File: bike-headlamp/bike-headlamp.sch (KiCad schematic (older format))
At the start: 9 parts, among them P1 Harness Connection, P2 HEADSET, P3 LED1, P4 LED2, SW1 RED, SW2 WHITE, SW3 DIM, U1 BUCKPUCK-3021-D-E-700, U2 Trinket

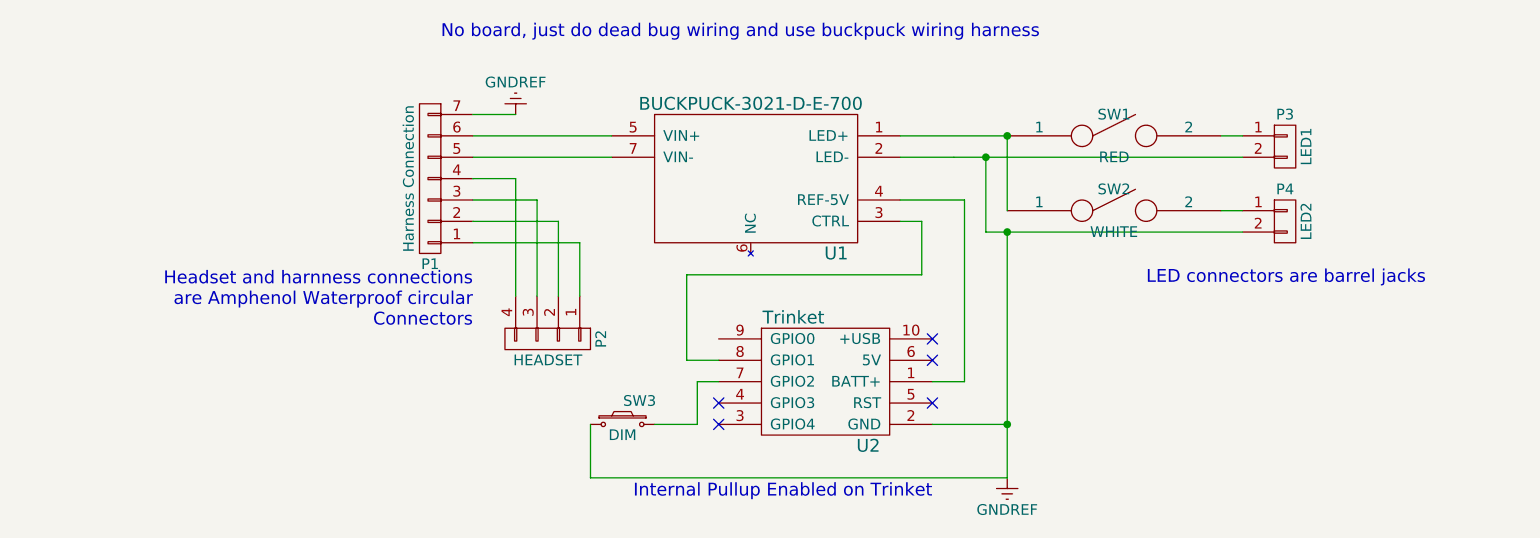
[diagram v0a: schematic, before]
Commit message: added strobe switch
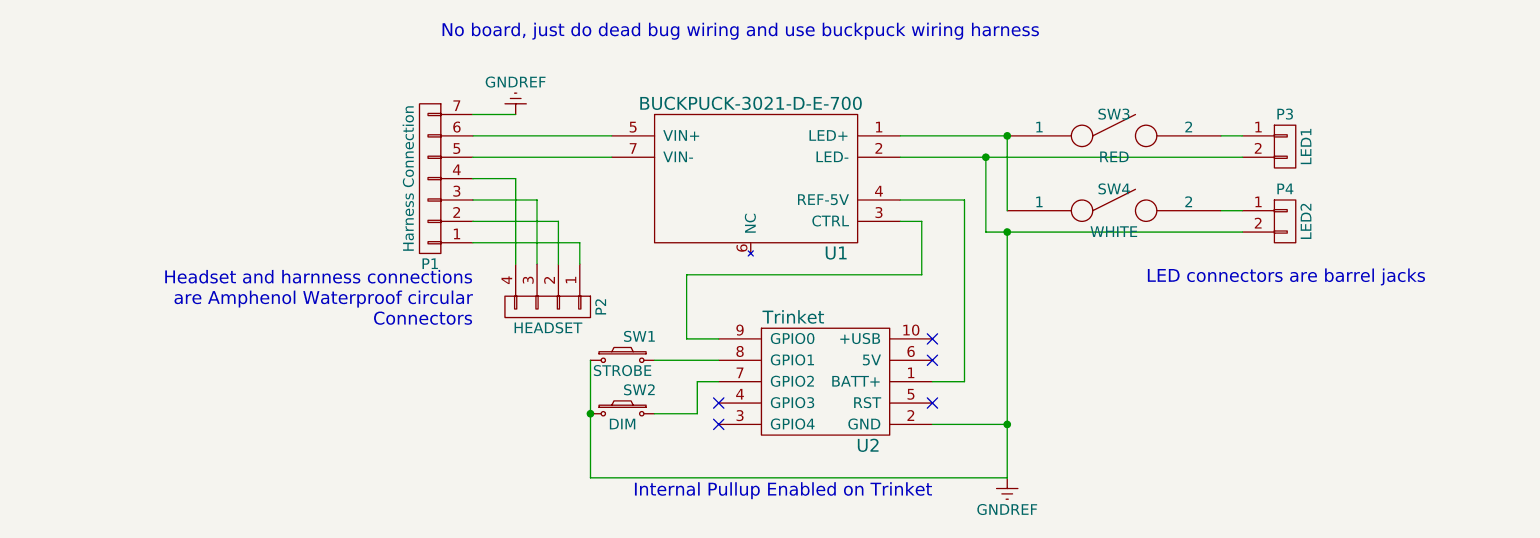
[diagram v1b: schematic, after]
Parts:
- added SW1: STROBE, symbol SW_PUSH_SMALL_H
- renumbered SW3 to SW2, SW1 to SW3, SW2 to SW4
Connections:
- net GNDREF: now also SW1.1
- net at U1.3 (CTRL): now also U2.9 (GPIO0); no longer U2.8 (GPIO1)
- new net: SW1.2, U2.8 (GPIO1)
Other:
- moved on the sheet: P2, SW2
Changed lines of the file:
@@
 L CONN_01X04 P2
 U 1 1 584A6F70
-P 4350 3750
-F 0 "P2" H 4350 4000 50  0000 C CNN
-F 1 "HEADSET" V 4450 3750 50  0000 C CNN
-F 2 "" H 4350 3750 50  0000 C CNN
-F 3 "" H 4350 3750 50  0000 C CNN
-	1    4350 3750
+P 4350 3600
+F 0 "P2" H 4350 3850 50  0000 C CNN
+F 1 "HEADSET" V 4450 3600 50  0000 C CNN
+F 2 "" H 4350 3600 50  0000 C CNN
+F 3 "" H 4350 3600 50  0000 C CNN
+	1    4350 3600
 	0    1    1    0
 $EndComp
@@
 	6000 2800 6500 2800
 Wire Wire Line
-	6000 2900 6250 2900
-Wire Wire Line
-	6250 2900 6400 2900
-Wire Wire Line
-	6400 2900 7600 2900
+	6000 2900 7600 2900
 Wire Wire Line
 	6500 2800 6500 3150
 Connection ~ 6500 2800
 Wire Wire Line
-	6400 3250 6500 3250
-Wire Wire Line
-	6500 3250 7600 3250
+	6400 3250 7600 3250
 Wire Wire Line
 	6400 3250 6400 2900
@@
 	4000 3000 4200 3000
 Wire Wire Line
-	4200 3000 4200 3550
+	4200 3000 4200 3400
 Wire Wire Line
 	4000 3100 4300 3100
 Wire Wire Line
-	4300 3100 4300 3550
+	4300 3100 4300 3400
 Wire Wire Line
 	4000 3200 4400 3200
 Wire Wire Line
-	4400 3200 4400 3550
+	4400 3200 4400 3400
 Wire Wire Line
 	4000 3300 4500 3300
 Wire Wire Line
-	4500 3300 4500 3550
+	4500 3300 4500 3400
 Wire Wire Line
 	4000 2700 4200 2700
@@
 	6150 4150 6500 4150
 Wire Wire Line
-	6500 3250 6500 4150
-Wire Wire Line
-	6500 4150 6500 4400
+	6500 3250 6500 4400
 Connection ~ 6500 3250
 NoConn ~ 6150 3750
@@
 NoConn ~ 5150 4150
 $Comp
-L SW_PUSH_SMALL_H SW3
+L SW_PUSH_SMALL_H SW2
 U 1 1 584A888C
-P 4700 4150
-F 0 "SW3" H 4780 4260 50  0000 C CNN
-F 1 "DIM" H 4700 4100 50  0000 C CNN
-F 2 "" H 4700 4350 50  0000 C CNN
-F 3 "" H 4700 4350 50  0000 C CNN
-	1    4700 4150
+P 4700 4100
+F 0 "SW2" H 4780 4210 50  0000 C CNN
+F 1 "DIM" H 4700 4050 50  0000 C CNN
+F 2 "" H 4700 4300 50  0000 C CNN
+F 3 "" H 4700 4300 50  0000 C CNN
+	1    4700 4100
 	1    0    0    -1
 $EndComp
@@
 	5150 3950 5050 3950
 Wire Wire Line
-	5050 3950 5050 4150
-Wire Wire Line
-	5050 4150 4850 4150
-Wire Wire Line
-	6500 4400 4550 4400
+	5050 3950 5050 4100
+Wire Wire Line
+	5050 4100 4850 4100
+Wire Wire Line
+	4550 4400 6500 4400
 Connection ~ 6500 4150
 NoConn ~ 6150 4050
@@
 No board, just do dead bug wiring and use buckpuck wiring harness
 Wire Wire Line
-	4550 4400 4550 4150
+	4550 3850 4550 4400
 Wire Wire Line
 	6000 3200 6100 3200
@@
 Wire Wire Line
 	6100 3450 5000 3450
-Wire Wire Line
-	5000 3450 5000 3850
-Wire Wire Line
-	5000 3850 5150 3850
-$Comp
-L SPST SW1
+$Comp
+L SPST SW3
 U 1 1 584B170A
 P 7000 2800
-F 0 "SW1" H 7000 2900 50  0000 C CNN
+F 0 "SW3" H 7000 2900 50  0000 C CNN
 F 1 "RED" H 7000 2700 50  0000 C CNN
 F 2 "" H 7000 2800 50  0000 C CNN
@@
 $EndComp
 $Comp
-L SPST SW2
+L SPST SW4
 U 1 1 584B175D
 P 7000 3150
-F 0 "SW2" H 7000 3250 50  0000 C CNN
+F 0 "SW4" H 7000 3250 50  0000 C CNN
 F 1 "WHITE" H 7000 3050 50  0000 C CNN
 F 2 "" H 7000 3150 50  0000 C CNN
@@
 Text Notes 4000 3700 2    60   ~ 0
 Headset and harnness connections\nare Amphenol Waterproof circular\nConnectors
+$Comp
+L SW_PUSH_SMALL_H SW1
+U 1 1 584CC69D
+P 4700 3850
+F 0 "SW1" H 4780 3960 50  0000 C CNN
+F 1 "STROBE" H 4700 3800 50  0000 C CNN
+F 2 "" H 4700 4050 50  0000 C CNN
+F 3 "" H 4700 4050 50  0000 C CNN
+	1    4700 3850
+	1    0    0    -1
+$EndComp
+Wire Wire Line
+	5150 3750 5000 3750
+Wire Wire Line
+	5000 3750 5000 3450
+Wire Wire Line
+	5150 3850 4850 3850
+Connection ~ 4550 4100
 $EndSCHEMATC

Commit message: Modified schematic for use with minipuck and new design
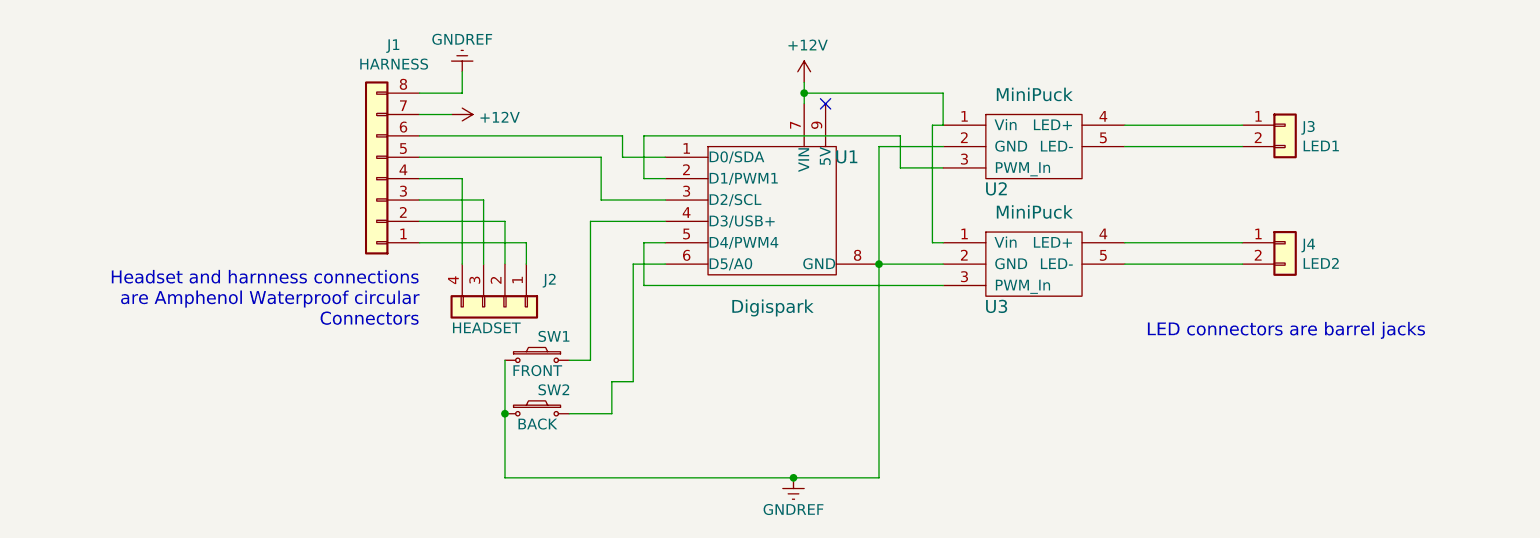
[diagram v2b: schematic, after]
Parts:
- removed P1: Harness Connection, symbol CONN_01X07
- removed P2: HEADSET, symbol CONN_01X04
- removed P3: LED1, symbol CONN_01X02
- removed P4: LED2, symbol CONN_01X02
- removed SW3: RED, symbol SPST
- removed SW4: WHITE, symbol SPST
- removed U1: BUCKPUCK-3021-D-E-700, 700mA 12-32V, symbol BUCKPUCK-3021-D-E
- removed U2: Trinket, symbol Trinket
- added J1: HARNESS, symbol Conn_01x08
- added J2: HEADSET, symbol Conn_01x04
- added J3: LED1, symbol Conn_01x02
- added J4: LED2, symbol Conn_01x02
- added U1: Digispark, SW-Digistump:Digispark, symbol Digispark
- added U2, U3: MiniPuck, symbol MiniPuck
- SW1: value STROBE -> FRONT
- SW2: value DIM -> BACK
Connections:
- net GNDREF: now also J1.8 (Pin_8), U1.8 (GND), U2.2 (GND), U3.2 (GND)
- net at SW2.2: now also U1.6 (D5/A0)
- net at SW1.2: now also U1.4 (D3/USB+)
- new net: J1.1 (Pin_1), J2.1 (Pin_1)
- new net: J1.2 (Pin_2), J2.2 (Pin_2)
- new net: J1.3 (Pin_3), J2.3 (Pin_3)
- new net: J1.4 (Pin_4), J2.4 (Pin_4)
- new net: J1.5 (Pin_5), U1.3 (D2/SCL)
- new net: J1.6 (Pin_6), U1.1 (D0/SDA)
- new net: U1.2 (D1/PWM1), U2.3 (PWM_In)
- new net: J3.1 (Pin_1), U2.4 (LED+)
- new net: J3.2 (Pin_2), U2.5 (LED-)
- new net: U1.5 (D4/PWM4), U3.3 (PWM_In)
- new net: J4.1 (Pin_1), U3.4 (LED+)
- new net: J4.2 (Pin_2), U3.5 (LED-)
- new net +12V: J1.7 (Pin_7), U1.7 (VIN), U2.1 (Vin), U3.1 (Vin)
- no-connect marks 5 -> 1
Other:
- note removed: "Internal Pullup Enabled on Trinket"
- note removed: "No board, just do dead bug wiring and use buckpuck wiring harness"
- moved on the sheet: SW1, SW2

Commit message: starting pcb layout
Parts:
- J1: footprint (none) -> Pin_Headers:Pin_Header_Straight_1x08_Pitch2.54mm; Description (none) -> Waterproof Circular Connector; Manufacturer (none) -> Amphenol LTW; Package ID (none) -> BD-08RMMS-SC7001; Pricing (none) -> 0.00@0
- J2: footprint (none) -> Pin_Headers:Pin_Header_Straight_1x04_Pitch2.54mm; Description (none) -> Waterproof Circular Connector; Manufacturer (none) -> Amphenol LTW; Package ID (none) -> AU-04RMMS-SC7001; Pricing (none) -> 0.00@0
- J3, J4: footprint (none) -> Pin_Headers:Pin_Header_Straight_1x02_Pitch2.54mm; Description (none) -> Barrel Jack; Manufacturer (none) -> Switchcraft; Package ID (none) -> 712AH; Pricing (none) -> 0.00@0
- SW1: footprint (none) -> Buttons_Switches_SMD:SW_SPST_PTS810; Characteristics (none) -> 125mA 125VAC; 100mA 50VDC, 500,000 Cycles at Full Load, 50m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; Description (none) -> Waterproof SPST Momentary pushbutton switch; Manufacturer (none) -> E-Switch; Package ID (none) -> RP8100B2M1CEBLKWHTNIL; Pricing (none) -> 0.00@0
- SW2: footprint (none) -> Buttons_Switches_SMD:SW_SPST_PTS810; Characteristics (none) -> 125mA 125VAC; 100mA 50VDC, 500,000 Cycles at Full Load, 50m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; Description (none) -> Waterproof SPST Momentary pushbutton switch; Manufacturer (none) -> E-Switch; Package ID (none) -> RP8100B2M1CEBLKREDNIL; Pricing (none) -> 0.00@0
- U2, U3: footprint (none) -> SW-LEDdynamics:MiniPuck-Pinned
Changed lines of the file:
@@
 F 0 "SW2" H 4380 4210 50  0000 C CNN
 F 1 "BACK" H 4300 4050 50  0000 C CNN
-F 2 "" H 4300 4300 50  0000 C CNN
+F 2 "Buttons_Switches_SMD:SW_SPST_PTS810" H 4300 4300 50  0001 C CNN
 F 3 "" H 4300 4300 50  0000 C CNN
+F 4 "125mA 125VAC; 100mA 50VDC, 500,000 Cycles at Full Load, 50mΩ Max. (Initial)" H 4300 4100 60  0001 C CNN "Characteristics"
+F 5 "E-Switch" H 4300 4100 60  0001 C CNN "Manufacturer"
+F 6 "Waterproof SPST Momentary pushbutton switch" H 4300 4100 60  0001 C CNN "Description"
+F 7 "RP8100B2M1CEBLKREDNIL" H 4300 4100 60  0001 C CNN "Package ID"
+F 8 "0.00@0" H 4300 4100 60  0001 C CNN "Pricing"
 	1    4300 4100
 	1    0    0    -1
@@
 	4650 4100 4450 4100
 Wire Wire Line
-	4150 4400 5500 4400
-Wire Wire Line
-	5500 4400 5900 4400
-Wire Wire Line
-	4150 3850 4150 4100
-Wire Wire Line
-	4150 4100 4150 4400
+	5900 4400 4150 4400
+Wire Wire Line
+	4150 4400 4150 3850
 Text Notes 7150 3750 0    60   ~ 0
 LED connectors are barrel jacks
@@
 F 0 "SW1" H 4380 3960 50  0000 C CNN
 F 1 "FRONT" H 4300 3800 50  0000 C CNN
-F 2 "" H 4300 4050 50  0000 C CNN
+F 2 "Buttons_Switches_SMD:SW_SPST_PTS810" H 4300 4050 50  0001 C CNN
 F 3 "" H 4300 4050 50  0000 C CNN
+F 4 "125mA 125VAC; 100mA 50VDC, 500,000 Cycles at Full Load, 50mΩ Max. (Initial)" H 4300 3850 60  0001 C CNN "Characteristics"
+F 5 "E-Switch" H 4300 3850 60  0001 C CNN "Manufacturer"
+F 6 "Waterproof SPST Momentary pushbutton switch" H 4300 3850 60  0001 C CNN "Description"
+F 7 "RP8100B2M1CEBLKWHTNIL" H 4300 3850 60  0001 C CNN "Package ID"
+F 8 "0.00@0" H 4300 3850 60  0001 C CNN "Pricing"
 	1    4300 3850
 	1    0    0    -1
@@
 F 0 "J1" H 3470 2375 50  0000 C CNN
 F 1 "HARNESS" H 3470 2466 50  0000 C CNN
-F 2 "" H 3550 3000 50  0001 C CNN
+F 2 "Pin_Headers:Pin_Header_Straight_1x08_Pitch2.54mm" H 3550 3000 50  0001 C CNN
 F 3 "" H 3550 3000 50  0001 C CNN
+F 4 "Amphenol LTW" H 3550 3000 60  0001 C CNN "Manufacturer"
+F 5 "Waterproof Circular Connector" H 3550 3000 60  0001 C CNN "Description"
+F 6 "BD-08RMMS-SC7001" H 3550 3000 60  0001 C CNN "Package ID"
+F 7 "0.00@0" H 3550 3000 60  0001 C CNN "Pricing"
 	1    3550 3000
 	-1   0    0    1
@@
 F 0 "U2" H 6450 2650 60  0000 C CNN
 F 1 "MiniPuck" H 6625 3091 60  0000 C CNN
-F 2 "" H 6350 2550 60  0001 C CNN
+F 2 "SW-LEDdynamics:MiniPuck-Pinned" H 6350 2550 60  0001 C CNN
 F 3 "" H 6450 2650 60  0001 C CNN
 F 4 "0.00@0" H 6600 3450 60  0001 C CNN "Pricing"
@@
 F 0 "U3" H 6450 3200 60  0000 C CNN
 F 1 "MiniPuck" H 6625 3641 60  0000 C CNN
-F 2 "" H 6350 3100 60  0001 C CNN
+F 2 "SW-LEDdynamics:MiniPuck-Pinned" H 6350 3100 60  0001 C CNN
 F 3 "" H 6450 3200 60  0001 C CNN
 F 4 "0.00@0" H 6600 4000 60  0001 C CNN "Pricing"
@@
 	6200 3400 5900 3400
 Wire Wire Line
-	5900 4400 5900 3400
-Wire Wire Line
-	5900 3400 5900 2850
+	5900 2850 5900 4400
 Wire Wire Line
 	5900 2850 6200 2850
@@
 $EndComp
 Wire Wire Line
-	5550 2550 5550 2600
-Wire Wire Line
-	5550 2600 5550 2650
+	5550 2550 5550 2650
 Wire Wire Line
 	5550 2600 6200 2600
@@
 F 0 "J2" V 4023 3780 50  0000 L CNN
 F 1 "HEADSET" V 4250 3350 50  0000 L CNN
-F 2 "" H 4150 3600 50  0001 C CNN
+F 2 "Pin_Headers:Pin_Header_Straight_1x04_Pitch2.54mm" H 4150 3600 50  0001 C CNN
 F 3 "" H 4150 3600 50  0001 C CNN
+F 4 "Amphenol LTW" H 4150 3600 60  0001 C CNN "Manufacturer"
+F 5 "Waterproof Circular Connector" H 4150 3600 60  0001 C CNN "Description"
+F 6 "AU-04RMMS-SC7001" H 4150 3600 60  0001 C CNN "Package ID"
+F 7 "0.00@0" H 4150 3600 60  0001 C CNN "Pricing"
 	1    4150 3600
 	0    1    1    0
@@
 F 0 "J3" H 7880 2742 50  0000 L CNN
 F 1 "LED1" H 7880 2651 50  0000 L CNN
-F 2 "" H 7800 2750 50  0001 C CNN
+F 2 "Pin_Headers:Pin_Header_Straight_1x02_Pitch2.54mm" H 7800 2750 50  0001 C CNN
 F 3 "" H 7800 2750 50  0001 C CNN
+F 4 "Switchcraft" H 7800 2750 60  0001 C CNN "Manufacturer"
+F 5 "Barrel Jack" H 7800 2750 60  0001 C CNN "Description"
+F 6 "712AH" H 7800 2750 60  0001 C CNN "Package ID"
+F 7 "0.00@0" H 7800 2750 60  0001 C CNN "Pricing"
 	1    7800 2750
 	1    0    0    -1
@@
 F 0 "J4" H 7880 3292 50  0000 L CNN
 F 1 "LED2" H 7880 3201 50  0000 L CNN
-F 2 "" H 7800 3300 50  0001 C CNN
+F 2 "Pin_Headers:Pin_Header_Straight_1x02_Pitch2.54mm" H 7800 3300 50  0001 C CNN
 F 3 "" H 7800 3300 50  0001 C CNN
+F 4 "Switchcraft" H 7800 3300 60  0001 C CNN "Manufacturer"
+F 5 "Barrel Jack" H 7800 3300 60  0001 C CNN "Description"
+F 6 "712AH" H 7800 3300 60  0001 C CNN "Package ID"
+F 7 "0.00@0" H 7800 3300 60  0001 C CNN "Pricing"
 	1    7800 3300
 	1    0    0    -1
 $EndComp
+$Comp
+L PWR_FLAG #FLG01
+U 1 1 59C36FA8
+P 5650 4400
+F 0 "#FLG01" H 5650 4475 50  0001 C CNN
+F 1 "PWR_FLAG" H 5650 4574 50  0000 C CNN
+F 2 "" H 5650 4400 50  0001 C CNN
+F 3 "" H 5650 4400 50  0001 C CNN
+	1    5650 4400
+	1    0    0    -1
+$EndComp
+$Comp
+L PWR_FLAG #FLG02
+U 1 1 59C36FCC
+P 5900 2600
+F 0 "#FLG02" H 5900 2675 50  0001 C CNN
+F 1 "PWR_FLAG" H 5900 2774 50  0000 C CNN
+F 2 "" H 5900 2600 50  0001 C CNN
+F 3 "" H 5900 2600 50  0001 C CNN
+	1    5900 2600
+	1    0    0    -1
+$EndComp
+Connection ~ 5900 2600
+Connection ~ 5650 4400
 $EndSCHEMATC

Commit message: finalized board?
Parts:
- removed J1: HARNESS, Pin_Headers:Pin_Header_Straight_1x08_Pitch2.54mm, symbol Conn_01x08
- added J1: HARNESS5-8, Pin_Headers:Pin_Header_Straight_1x04_Pitch2.54mm, symbol Conn_01x04
- added J2: HARNESS1-4, Pin_Headers:Pin_Header_Straight_1x04_Pitch2.54mm, symbol Conn_01x04
- SW1, SW2: footprint Buttons_Switches_SMD:SW_SPST_PTS810 -> Pin_Headers:Pin_Header_Straight_1x02_Pitch2.54mm
- renumbered J2 to J3, J3 to J4, J4 to J5
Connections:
- net +12V: now also J1.3 (Pin_3)
- net GNDREF: now also J1.4 (Pin_4)
- net SW-BACK: now reaches SW2.2, U1.6 (D5/A0)
- net SW-FRONT: now reaches SW1.2, U1.4 (D3/USB+)
- net at J3.1 (Pin_1): now also J2.1 (Pin_1)
- net at J3.2 (Pin_2): now also J2.2 (Pin_2)
- net at J3.3 (Pin_3): now also J2.3 (Pin_3)
- net at J3.4 (Pin_4): now also J2.4 (Pin_4)
- net SCL: now reaches U1.3 (D2/SCL)
- net SCL: now also J1.1 (Pin_1)
- net SDA: now reaches U1.1 (D0/SDA)
- net SDA: now also J1.2 (Pin_2)
- net LED1-PWM: now reaches U1.2 (D1/PWM1), U2.3 (PWM_In)
- net LED1+: now reaches J4.1 (Pin_1), U2.4 (LED+)
- net LED1-: now reaches J4.2 (Pin_2), U2.5 (LED-)
- net LED2-PWM: now reaches U1.5 (D4/PWM4), U3.3 (PWM_In)
- net LED2+: now reaches J5.1 (Pin_1), U3.4 (LED+)
- net LED2-: now reaches J5.2 (Pin_2), U3.5 (LED-)
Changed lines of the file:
@@
 F 0 "SW2" H 4380 4210 50  0000 C CNN
 F 1 "BACK" H 4300 4050 50  0000 C CNN
-F 2 "Buttons_Switches_SMD:SW_SPST_PTS810" H 4300 4300 50  0001 C CNN
+F 2 "Pin_Headers:Pin_Header_Straight_1x02_Pitch2.54mm" H 4300 4300 50  0001 C CNN
 F 3 "" H 4300 4300 50  0000 C CNN
 F 4 "125mA 125VAC; 100mA 50VDC, 500,000 Cycles at Full Load, 50mΩ Max. (Initial)" H 4300 4100 60  0001 C CNN "Characteristics"
@@
 F 0 "SW1" H 4380 3960 50  0000 C CNN
 F 1 "FRONT" H 4300 3800 50  0000 C CNN
-F 2 "Buttons_Switches_SMD:SW_SPST_PTS810" H 4300 4050 50  0001 C CNN
+F 2 "Pin_Headers:Pin_Header_Straight_1x02_Pitch2.54mm" H 4300 4050 50  0001 C CNN
 F 3 "" H 4300 4050 50  0000 C CNN
 F 4 "125mA 125VAC; 100mA 50VDC, 500,000 Cycles at Full Load, 50mΩ Max. (Initial)" H 4300 3850 60  0001 C CNN "Characteristics"
@@
 	4550 3850 4450 3850
 Connection ~ 4150 4100
-$Comp
-L Conn_01x08 J1
-U 1 1 59C3506A
-P 3550 3000
-F 0 "J1" H 3470 2375 50  0000 C CNN
-F 1 "HARNESS" H 3470 2466 50  0000 C CNN
-F 2 "Pin_Headers:Pin_Header_Straight_1x08_Pitch2.54mm" H 3550 3000 50  0001 C CNN
-F 3 "" H 3550 3000 50  0001 C CNN
-F 4 "Amphenol LTW" H 3550 3000 60  0001 C CNN "Manufacturer"
-F 5 "Waterproof Circular Connector" H 3550 3000 60  0001 C CNN "Description"
-F 6 "BD-08RMMS-SC7001" H 3550 3000 60  0001 C CNN "Package ID"
-F 7 "0.00@0" H 3550 3000 60  0001 C CNN "Pricing"
-	1    3550 3000
-	-1   0    0    1
-$EndComp
 Wire Wire Line
 	3750 2600 3950 2600
@@
 NoConn ~ 5650 2650
 $Comp
-L Conn_01x04 J2
+L Conn_01x04 J3
 U 1 1 59C36710
 P 4150 3600
-F 0 "J2" V 4023 3780 50  0000 L CNN
+F 0 "J3" V 4023 3780 50  0000 L CNN
 F 1 "HEADSET" V 4250 3350 50  0000 L CNN
 F 2 "Pin_Headers:Pin_Header_Straight_1x04_Pitch2.54mm" H 4150 3600 50  0001 C CNN
@@
 $EndComp
 $Comp
-L Conn_01x02 J3
+L Conn_01x02 J4
 U 1 1 59C369DF
 P 7800 2750
-F 0 "J3" H 7880 2742 50  0000 L CNN
+F 0 "J4" H 7880 2742 50  0000 L CNN
 F 1 "LED1" H 7880 2651 50  0000 L CNN
 F 2 "Pin_Headers:Pin_Header_Straight_1x02_Pitch2.54mm" H 7800 2750 50  0001 C CNN
@@
 $EndComp
 $Comp
-L Conn_01x02 J4
+L Conn_01x02 J5
 U 1 1 59C36A25
 P 7800 3300
-F 0 "J4" H 7880 3292 50  0000 L CNN
+F 0 "J5" H 7880 3292 50  0000 L CNN
 F 1 "LED2" H 7880 3201 50  0000 L CNN
 F 2 "Pin_Headers:Pin_Header_Straight_1x02_Pitch2.54mm" H 7800 3300 50  0001 C CNN
@@
 Connection ~ 5900 2600
 Connection ~ 5650 4400
+$Comp
+L Conn_01x04 J2
+U 1 1 59C37DF9
+P 3550 3200
+F 0 "J2" V 3423 3380 50  0000 L CNN
+F 1 "HARNESS1-4" V 3650 2950 50  0000 L CNN
+F 2 "Pin_Headers:Pin_Header_Straight_1x04_Pitch2.54mm" H 3550 3200 50  0001 C CNN
+F 3 "" H 3550 3200 50  0001 C CNN
+F 4 "Amphenol LTW" H 3550 3200 60  0001 C CNN "Manufacturer"
+F 5 "Waterproof Circular Connector" H 3550 3200 60  0001 C CNN "Description"
+F 6 "AU-04RMMS-SC7001" H 3550 3200 60  0001 C CNN "Package ID"
+F 7 "0.00@0" H 3550 3200 60  0001 C CNN "Pricing"
+	1    3550 3200
+	-1   0    0    1
+$EndComp
+$Comp
+L Conn_01x04 J1
+U 1 1 59C37E48
+P 3550 2800
+F 0 "J1" V 3423 2980 50  0000 L CNN
+F 1 "HARNESS5-8" V 3650 2550 50  0000 L CNN
+F 2 "Pin_Headers:Pin_Header_Straight_1x04_Pitch2.54mm" H 3550 2800 50  0001 C CNN
+F 3 "" H 3550 2800 50  0001 C CNN
+F 4 "Amphenol LTW" H 3550 2800 60  0001 C CNN "Manufacturer"
+F 5 "Waterproof Circular Connector" H 3550 2800 60  0001 C CNN "Description"
+F 6 "AU-04RMMS-SC7001" H 3550 2800 60  0001 C CNN "Package ID"
+F 7 "0.00@0" H 3550 2800 60  0001 C CNN "Pricing"
+	1    3550 2800
+	-1   0    0    1
+$EndComp
+Text Label 7100 2750 0    60   ~ 0
+LED1+
+Text Label 7100 2850 0    60   ~ 0
+LED1-
+Text Label 7100 3300 0    60   ~ 0
+LED2+
+Text Label 7100 3400 0    60   ~ 0
+LED2-
+Text Label 5100 2800 0    60   ~ 0
+LED1-PWM
+Text Label 5450 3500 2    60   ~ 0
+LED2-PWM
+Text Label 4250 2800 0    60   ~ 0
+SDA
+Text Label 4250 2900 0    60   ~ 0
+SCL
+Text Label 4750 3850 0    60   ~ 0
+SW-BACK
+Text Label 4550 3750 0    60   ~ 0
+SW-FRONT
 $EndSCHEMATC
